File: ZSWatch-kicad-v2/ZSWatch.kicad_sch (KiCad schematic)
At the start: 74 parts, among them IC1 ESDALC6V1W5, IC2 XC9265C181MR-G, IC3 TPS61023DRLT, IC4 MAX30101EFD+T, IC5 FAN5622SX, IC6 BMI270, IC7 LIS2MDLTR, IC8 AT25SF128A-MHB-T, J2 Charger and programming heade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, M1 Vibrator DC Motor, U1 MAX1811ESA+, U10 0_NORA-B106, U11 NTS0104GU12, U13 GC9A01A_CST816S, U2 DMC2400UV-7, U3 NCV300LSN36T1G, U4 BMP581, U5 BME688, U6 DRV2603RUNT, U7 XC9265A331MR-G

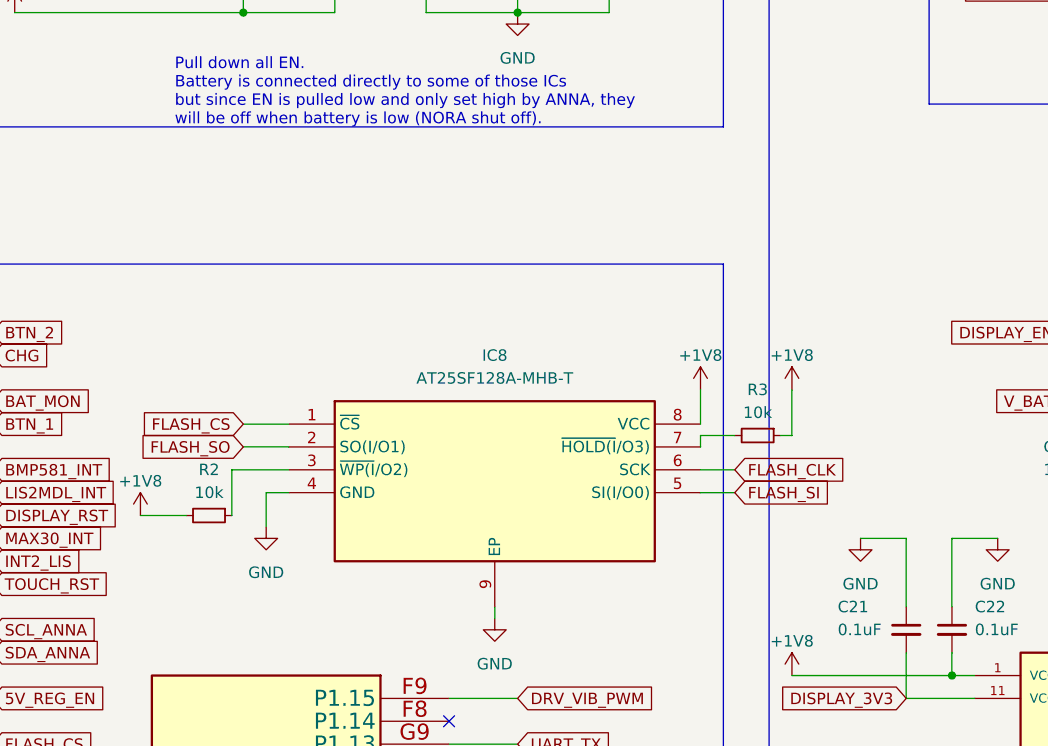
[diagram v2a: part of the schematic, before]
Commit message: Updated flash pcb design, with DRC rule fixes.
- Lowered down silkscreen of ZWatch to add test points to SPI for testing.
- Ground pad of flash is connected but is not necessary and can be removed
to simplify connections.
- Due to size constraints added 0402 resistors for pull up resistors on the left side
of the flash.
- Pending, change name of FLASH in Kicad to AT25SL128A.
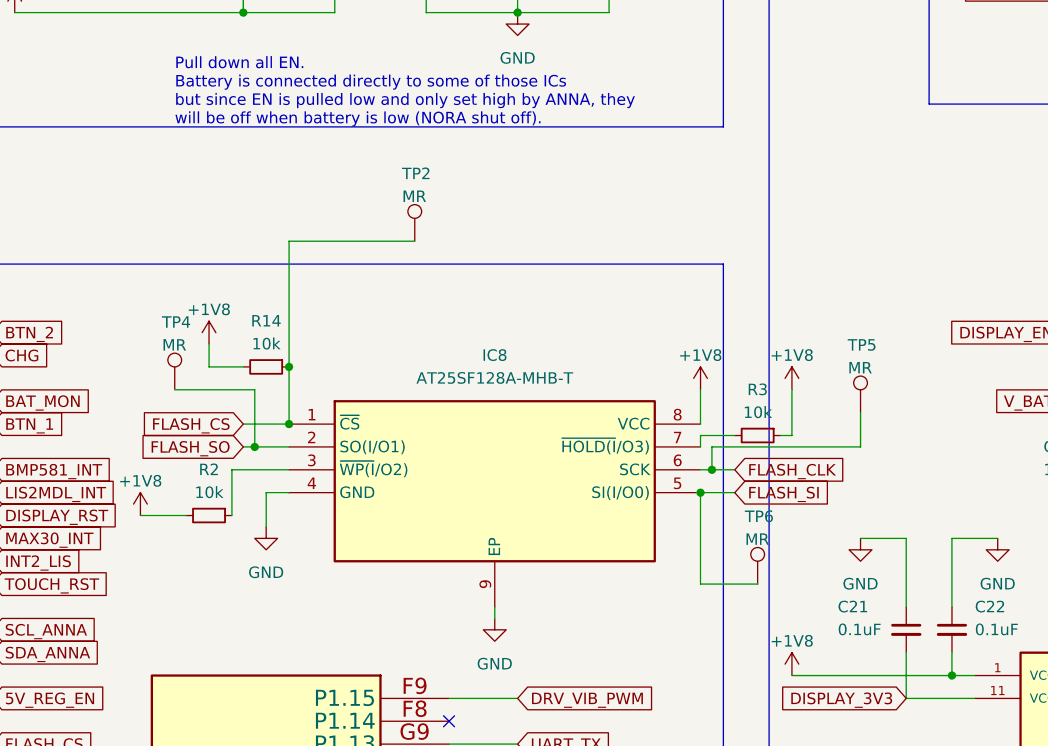
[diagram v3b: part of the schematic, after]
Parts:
- added R14: 10k, Resistor_SMD:R_0402_1005Metric, symbol Device:R_Small
- added TP2, TP4, TP5, TP6: MR, TestPoint:TestPoint_Pad_D1.0mm, symbol Connector:TestPoint
- R2: footprint Resistor_SMD:R_0603_1608Metric -> Resistor_SMD:R_0402_1005Metric
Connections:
- net +1V8: now also R14.2
- net FLASH_CLK: now also TP5.1
- net FLASH_CS: now also R14.1, TP2.1
- net FLASH_SI: now also TP6.1
- net FLASH_SO: now also TP4.1
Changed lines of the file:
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@@
   (junction (at 264.16 96.52) (diameter 0) (color 0 0 0 0)
   )
+  (junction (at 182.88 203.2) (diameter 0) (color 0 0 0 0)
+  )
   (junction (at 104.14 81.28) (diameter 0) (color 0 0 0 0)
   )
@@
   (junction (at 109.22 88.9) (diameter 0) (color 0 0 0 0)
   )
+  (junction (at 228.6 210.82) (diameter 0) (color 0 0 0 0)
+  )
   (junction (at 419.1 182.88) (diameter 0) (color 0 0 0 0)
   )
@@
   (junction (at 467.36 198.12) (diameter 0) (color 0 0 0 0)
   )
+  (junction (at 229.87 208.28) (diameter 0) (color 0 0 0 0)
+  )
   (junction (at 467.36 231.14) (diameter 0) (color 0 0 0 0)
   )
@@
   (junction (at 467.36 144.78) (diameter 0) (color 0 0 0 0)
   )
+  (junction (at 182.88 196.85) (diameter 0) (color 0 0 0 0)
+  )
   (junction (at 480.06 198.12) (diameter 0) (color 0 0 0 0)
   )
@@
   (junction (at 160.02 101.6) (diameter 0) (color 0 0 0 0)
   )
+  (junction (at 179.07 205.74) (diameter 0) (color 0 0 0 0)
+  )
   (junction (at 457.2 231.14) (diameter 0) (color 0 0 0 0)
   )
@@
     (stroke (width 0) (type default))
   )
+  (wire (pts (xy 234.95 220.98) (xy 228.6 220.98))
+    (stroke (width 0) (type default))
+  )
   (wire (pts (xy 459.74 162.56) (xy 474.98 162.56))
     (stroke (width 0) (type default))
@@
     (stroke (width 0) (type default))
   )
-  (wire (pts (xy 177.8 205.74) (xy 182.88 205.74))
+  (wire (pts (xy 177.8 205.74) (xy 179.07 205.74))
     (stroke (width 0) (type default))
   )
@@
     (stroke (width 0) (type default))
   )
+  (wire (pts (xy 246.38 201.93) (xy 246.38 205.74))
+    (stroke (width 0) (type default))
+  )
   (wire (pts (xy 266.7 284.48) (xy 271.78 284.48))
     (stroke (width 0) (type default))
@@
     (stroke (width 0) (type default))
   )
+  (wire (pts (xy 182.88 182.88) (xy 182.88 196.85))
+    (stroke (width 0) (type default))
+  )
   (wire (pts (xy 176.53 208.28) (xy 182.88 208.28))
     (stroke (width 0) (type default))
@@
     (stroke (width 0) (type default))
   )
+  (wire (pts (xy 228.6 220.98) (xy 228.6 210.82))
+    (stroke (width 0) (type default))
+  )
   (wire (pts (xy 170.18 71.12) (xy 170.18 60.96))
     (stroke (width 0) (type default))
@@
     (stroke (width 0) (type default))
   )
+  (wire (pts (xy 229.87 208.28) (xy 232.41 208.28))
+    (stroke (width 0) (type default))
+  )
   (polyline (pts (xy 358.14 322.58) (xy 358.14 124.46))
     (stroke (width 0) (type default))
@@
     (stroke (width 0) (type default))
   )
-  (wire (pts (xy 228.6 208.28) (xy 232.41 208.28))
+  (wire (pts (xy 228.6 208.28) (xy 229.87 208.28))
     (stroke (width 0) (type default))
   )
@@
     (stroke (width 0) (type default))
   )
+  (wire (pts (xy 173.99 194.31) (xy 173.99 196.85))
+    (stroke (width 0) (type default))
+  )
+  (wire (pts (xy 246.38 205.74) (xy 229.87 205.74))
+    (stroke (width 0) (type default))
+  )
   (wire (pts (xy 63.5 165.1) (xy 63.5 170.18))
     (stroke (width 0) (type default))
@@
     (stroke (width 0) (type default))
   )
+  (wire (pts (xy 179.07 205.74) (xy 182.88 205.74))
+    (stroke (width 0) (type default))
+  )
   (wire (pts (xy 279.4 152.4) (xy 276.86 152.4))
     (stroke (width 0) (type default))
@@
     (stroke (width 0) (type default))
   )
+  (wire (pts (xy 179.07 199.39) (xy 179.07 205.74))
+    (stroke (width 0) (type default))
+  )
   (polyline (pts (xy 236.22 124.46) (xy 236.22 322.58))
     (stroke (width 0) (type default))
@@
     (stroke (width 0) (type default))
   )
+  (wire (pts (xy 229.87 205.74) (xy 229.87 208.28))
+    (stroke (width 0) (type default))
+  )
   (wire (pts (xy 472.44 228.6) (xy 477.52 228.6))
     (stroke (width 0) (type default))
@@
     (stroke (width 0) (type default))
   )
+  (wire (pts (xy 196.85 182.88) (xy 182.88 182.88))
+    (stroke (width 0) (type default))
+  )
   (wire (pts (xy 200.66 246.38) (xy 208.28 246.38))
     (stroke (width 0) (type default))
@@
     (stroke (width 0) (type default))
   )
+  (wire (pts (xy 173.99 196.85) (xy 177.8 196.85))
+    (stroke (width 0) (type default))
+  )
   (wire (pts (xy 309.88 287.02) (xy 309.88 289.56))
     (stroke (width 0) (type default))
@@
     (stroke (width 0) (type default))
   )
+  (wire (pts (xy 182.88 196.85) (xy 182.88 203.2))
+    (stroke (width 0) (type default))
+  )
   (wire (pts (xy 347.98 83.82) (xy 342.9 83.82))
     (stroke (width 0) (type default))
@@
     (stroke (width 0) (type default))
   )
+  (wire (pts (xy 170.18 199.39) (xy 179.07 199.39))
+    (stroke (width 0) (type default))
+  )
   (wire (pts (xy 454.66 243.84) (xy 467.36 243.84))
     (stroke (width 0) (type default))
@@
     )
   )
+  (symbol (lib_id "power:+1V8") (at 173.99 194.31 0) (unit 1)
+    (in_bom yes) (on_board yes) (dnp no) (fields_autoplaced)
+    (property "Reference" "#PWR017" (at 173.99 198.12 0)
+      (effects (font (size 1.27 1.27)) hide)
+    )
+    (property "Value" "+1V8" (at 173.99 190.5 0)
+      (effects (font (size 1.27 1.27)))
+    )
+    (property "Footprint" "" (at 173.99 194.31 0)
+      (effects (font (size 1.27 1.27)) hide)
+    )
+    (property "Datasheet" "" (at 173.99 194.31 0)
+      (effects (font (size 1.27 1.27)) hide)
+    )
+    (pin "1")
+    (instances
+      (project "ZSWatch"
+        (path "/d5742f03-3b1a-42e5-a384-018bd4b919aa"
+          (reference "#PWR017") (unit 1)
+        )
+      )
+    )
+  )
+  (symbol (lib_id "Connector:TestPoint") (at 196.85 182.88 0) (unit 1)
+    (in_bom yes) (on_board yes) (dnp no)
+    (property "Reference" "TP2" (at 195.435 175.3936 0)
+      (effects (font (size 1.27 1.27)) (justify left))
+    )
+    (property "Value" "MR" (at 195.435 177.9336 0)
+      (effects (font (size 1.27 1.27)) (justify left))
+    )
+    (property "Footprint" "TestPoint:TestPoint_Pad_D1.0mm" (at 201.93 182.88 0)
+      (effects (font (size 1.27 1.27)) hide)
+    )
+    (property "Datasheet" "~" (at 201.93 182.88 0)
+      (effects (font (size 1.27 1.27)) hide)
+    )
+    (pin "1")
+    (instances
+      (project "ZSWatch"
+        (path "/d5742f03-3b1a-42e5-a384-018bd4b919aa"
+          (reference "TP2") (unit 1)
+        )
+      )
+    )
+  )
   (symbol (lib_id "power:GND") (at 88.9 276.86 0) (unit 1)
     (in_bom yes) (on_board yes) (dnp no)
@@
     )
   )
+  (symbol (lib_id "Connector:TestPoint") (at 246.38 201.93 0) (unit 1)
+    (in_bom yes) (on_board yes) (dnp no)
+    (property "Reference" "TP5" (at 244.965 194.4436 0)
+      (effects (font (size 1.27 1.27)) (justify left))
+    )
+    (property "Value" "MR" (at 244.965 196.9836 0)
+      (effects (font (size 1.27 1.27)) (justify left))
+    )
+    (property "Footprint" "TestPoint:TestPoint_Pad_D1.0mm" (at 251.46 201.93 0)
+      (effects (font (size 1.27 1.27)) hide)
+    )
+    (property "Datasheet" "~" (at 251.46 201.93 0)
+      (effects (font (size 1.27 1.27)) hide)
+    )
+    (pin "1")
+    (instances
+      (project "ZSWatch"
+        (path "/d5742f03-3b1a-42e5-a384-018bd4b919aa"
+          (reference "TP5") (unit 1)
+        )
+      )
+    )
+  )
   (symbol (lib_id "Device:C_Small") (at 213.36 63.5 0) (unit 1)
     (in_bom yes) (on_board yes) (dnp no)
@@
     )
   )
+  (symbol (lib_id "Connector:TestPoint") (at 234.95 220.98 0) (unit 1)
+    (in_bom yes) (on_board yes) (dnp no)
+    (property "Reference" "TP6" (at 233.535 213.4936 0)
+      (effects (font (size 1.27 1.27)) (justify left))
+    )
+    (property "Value" "MR" (at 233.535 216.0336 0)
+      (effects (font (size 1.27 1.27)) (justify left))
+    )
+    (property "Footprint" "TestPoint:TestPoint_Pad_D1.0mm" (at 240.03 220.98 0)
+      (effects (font (size 1.27 1.27)) hide)
+    )
+    (property "Datasheet" "~" (at 240.03 220.98 0)
+      (effects (font (size 1.27 1.27)) hide)
+    )
+    (pin "1")
+    (instances
+      (project "ZSWatch"
+        (path "/d5742f03-3b1a-42e5-a384-018bd4b919aa"
+          (reference "TP6") (unit 1)
+        )
+      )
+    )
+  )
   (symbol (lib_id "power:GND") (at 457.2 210.82 0) (unit 1)
     (in_bom yes) (on_board yes) (dnp no)
@@
     )
   )
+  (symbol (lib_id "Device:R_Small") (at 180.34 196.85 270) (unit 1)
+    (in_bom yes) (on_board yes) (dnp no)
+    (property "Reference" "R14" (at 180.34 191.77 90)
+      (effects (font (size 1.27 1.27)))
+    )
+    (property "Value" "10k" (at 180.34 194.31 90)
+      (effects (font (size 1.27 1.27)))
+    )
+    (property "Footprint" "Resistor_SMD:R_0402_1005Metric" (at 180.34 196.85 0)
+      (effects (font (size 1.27 1.27)) hide)
+    )
+    (property "Datasheet" "~" (at 180.34 196.85 0)
+      (effects (font (size 1.27 1.27)) hide)
+    )
+    (pin "1")
+    (pin "2")
+    (instances
+      (project "ZSWatch"
+        (path "/d5742f03-3b1a-42e5-a384-018bd4b919aa"
+          (reference "R14") (unit 1)
+        )
+      )
+    )
+  )
   (symbol (lib_id "power:GND") (at 477.52 228.6 0) (unit 1)
     (in_bom yes) (on_board yes) (dnp no)
@@
       (effects (font (size 1.27 1.27)))
     )
-    (property "Footprint" "Resistor_SMD:R_0603_1608Metric" (at 173.99 213.36 0)
+    (property "Footprint" "Resistor_SMD:R_0402_1005Metric" (at 173.99 213.36 0)
       (effects (font (size 1.27 1.27)) hide)
     )
@@
         )
       )
+    )
+  )
+  (symbol (lib_id "Connector:TestPoint") (at 170.18 199.39 0) (unit 1)
+    (in_bom yes) (on_board yes) (dnp no)
+    (property "Reference" "TP4" (at 168.765 191.9036 0)
+      (effects (font (size 1.27 1.27)) (justify left))
+    )
+    (property "Value" "MR" (at 168.765 194.4436 0)
+      (effects (font (size 1.27 1.27)) (justify left))
+    )
+    (property "Footprint" "TestPoint:TestPoint_Pad_D1.0mm" (at 175.26 199.39 0)
+      (effects (font (size 1.27 1.27)) hide)
+    )
+    (property "Datasheet" "~" (at 175.26 199.39 0)
+      (effects (font (size 1.27 1.27)) hide)
+    )
+    (pin "1")
+    (instances
+      (project "ZSWatch"
+        (path "/d5742f03-3b1a-42e5-a384-018bd4b919aa"
+          (reference "TP4") (unit 1)
+        )
+      )

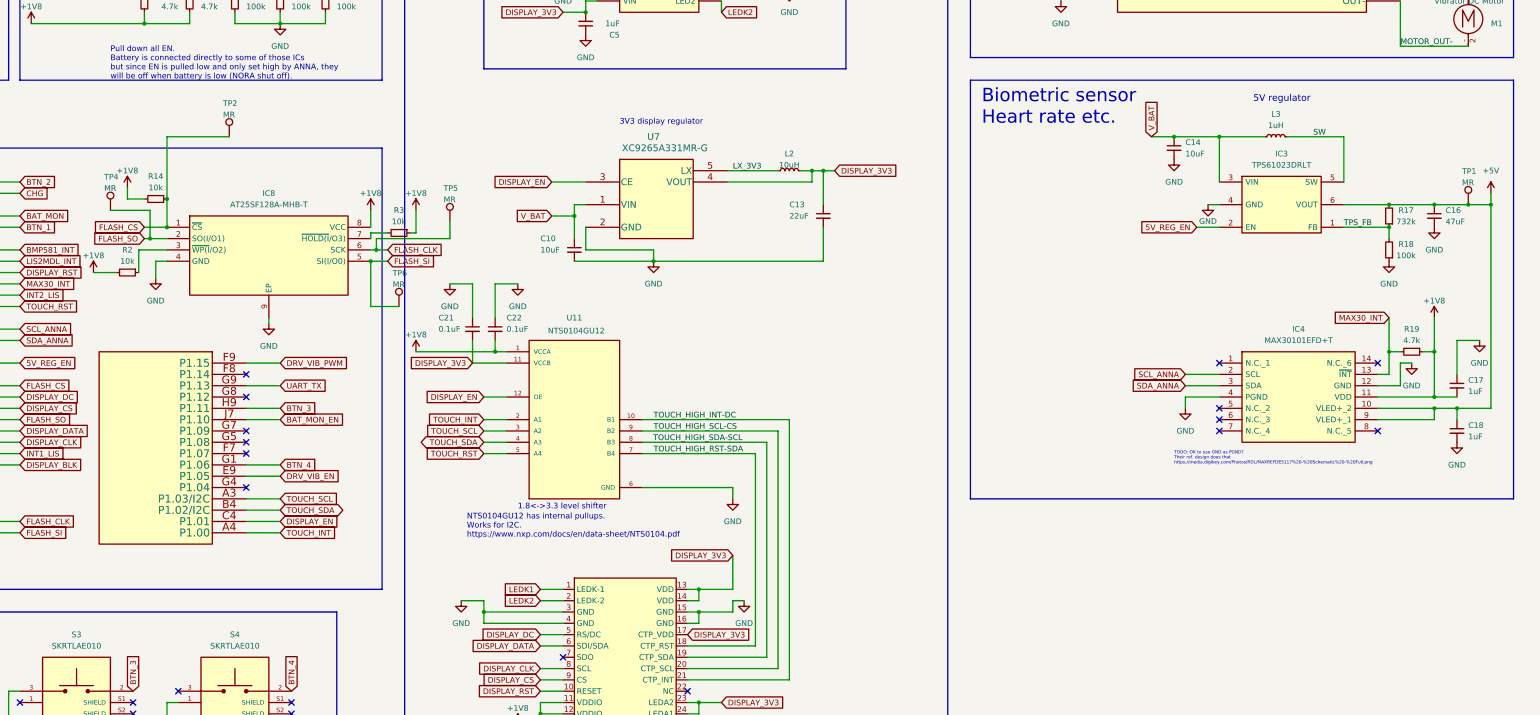
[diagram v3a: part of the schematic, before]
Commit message: PCB: Move draft flash schematic into its own section. Correct datasheet and model number of flash.
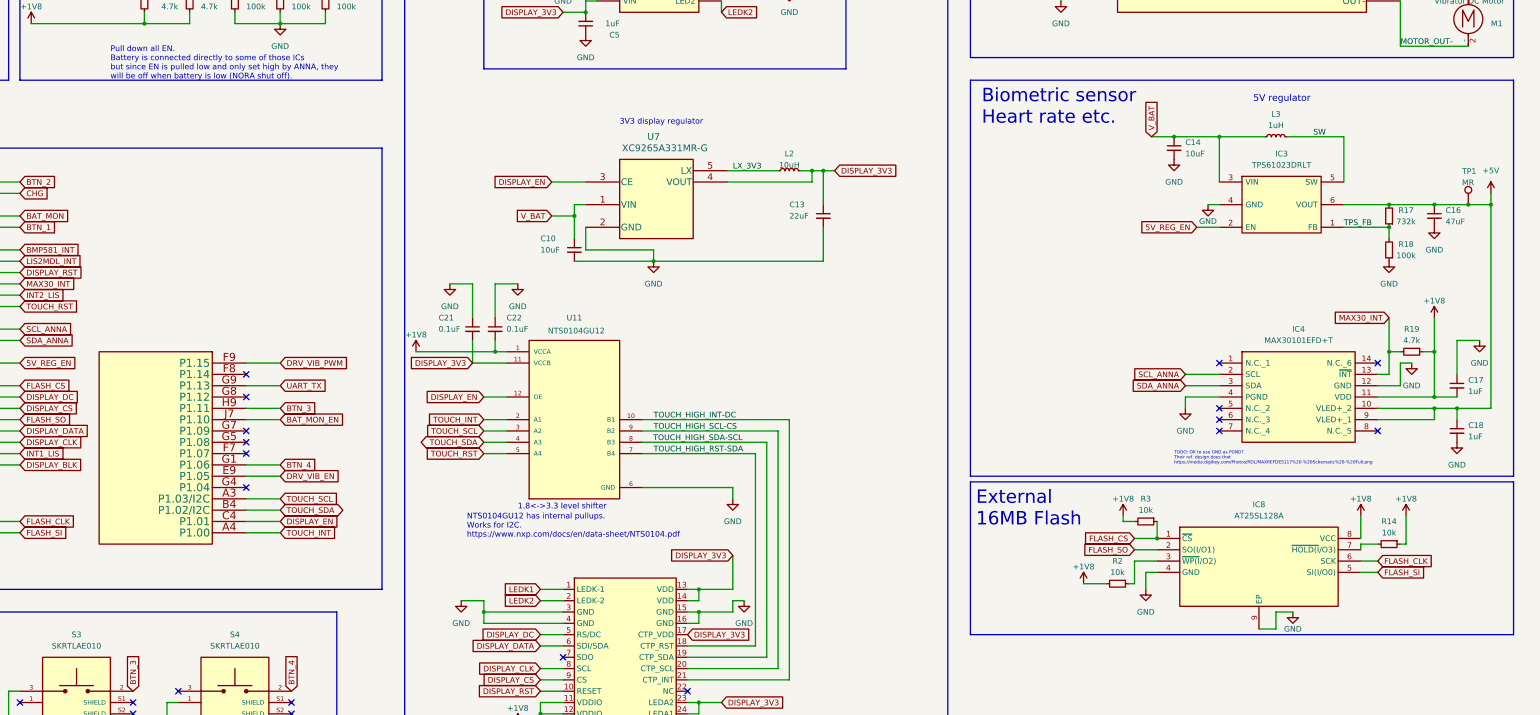
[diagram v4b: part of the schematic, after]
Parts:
- removed TP2, TP4, TP5, TP6: MR, TestPoint:TestPoint_Pad_D1.0mm, symbol Connector:TestPoint
- IC8: value AT25SF128A-MHB-T -> AT25SL128A; Manufacturer_Part_Number AT25SF128A-MHB-T -> 988-AT25SL128A-MHE-T; Mouser Part Number 988-AT25SF128A-MHB-T -> 988-AT25SL128A-MHE-T; Mouser Price/Stock https://www.mouser.co.uk/ProductDetail/Dialog-Semiconductor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 -> https://www.mouser.se/ProductDetail/Renesas-Dialog/AT25SL12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
- R14: footprint Resistor_SMD:R_0402_1005Metric -> Resistor_SMD:R_0603_1608Metric
- R3: footprint Resistor_SMD:R_0603_1608Metric -> Resistor_SMD:R_0402_1005Metric
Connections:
- net +1V8: now also R14.1, R3.2; no longer R14.2, R3.1
- net FLASH_CS: now also R3.1; no longer R14.1
- net at IC8.7 (~{HOLD(I}/O3)): now also R14.2; no longer R3.2
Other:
- note added: "External 16MB Flash"
